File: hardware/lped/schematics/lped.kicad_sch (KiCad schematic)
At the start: 29 parts, among them J1 3V3, J10 SWDIO, J2 DOCK_BUTTON, J3 DOCK_CONN, J4 DOCK_LED, J5 GND, J6 ~{RESET}, J9 SWDCLK, U1 nRF52810-QCxx, Y1 32MHz

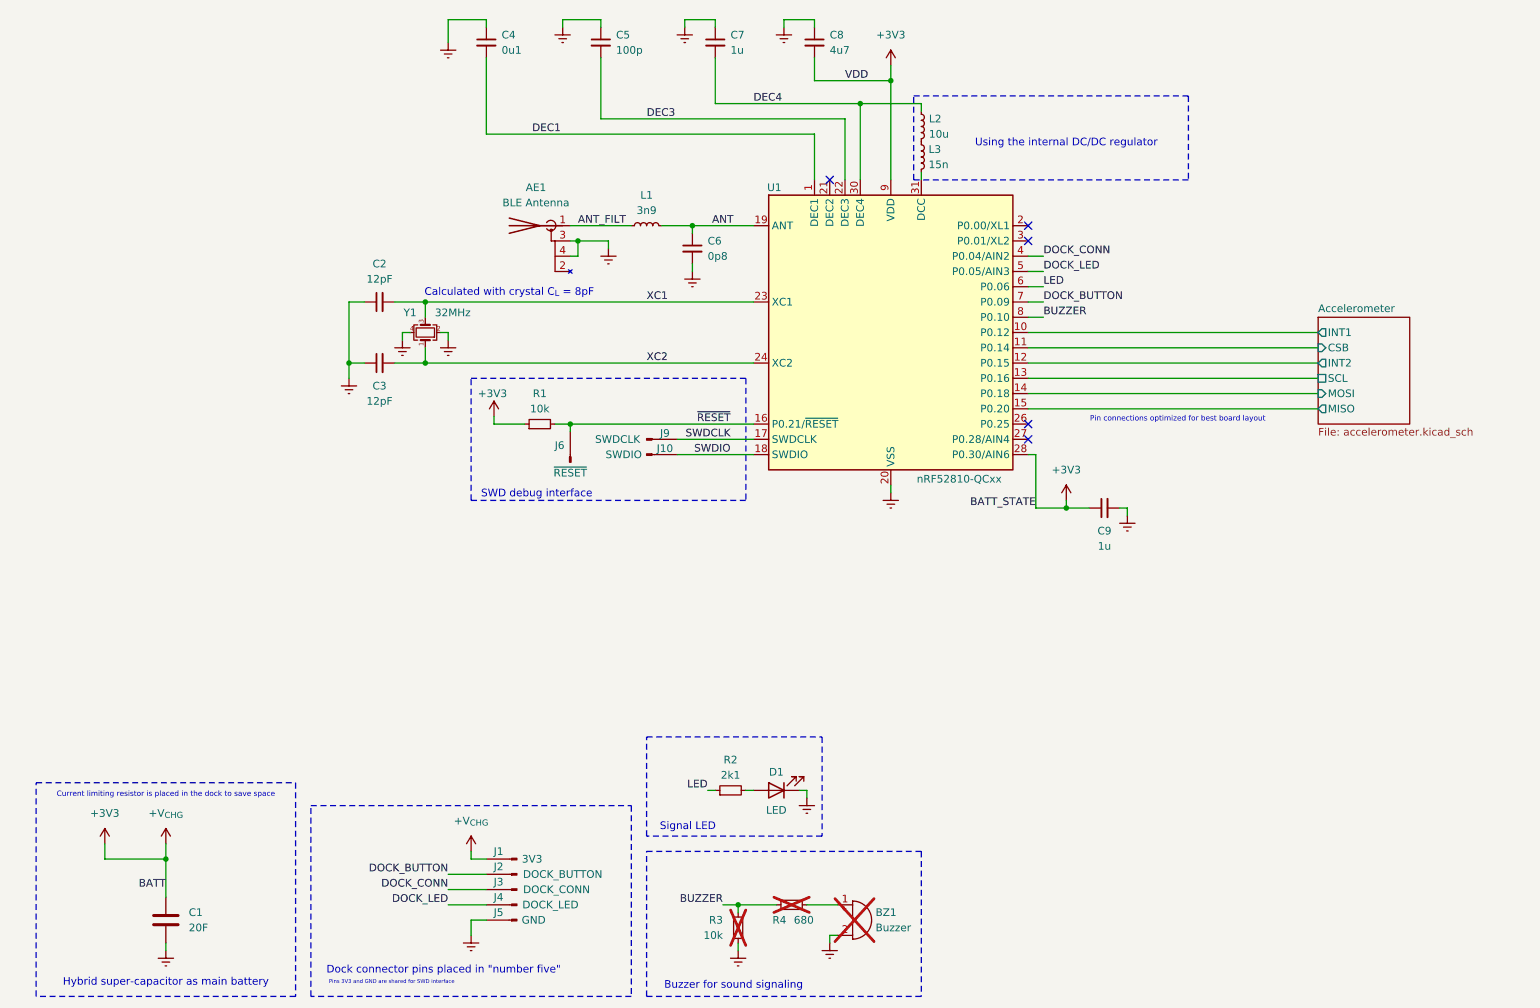
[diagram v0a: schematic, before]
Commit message: feat(hardware)!: v2 of LPED PCB
* Changed MCU to nRF52833 (from nRF52810)
* Added second LED
* Used specialized filter instead of discrete components for ANT
* Removed unnecessary pull-down resistor from miso
* Removed DOCK_BTN
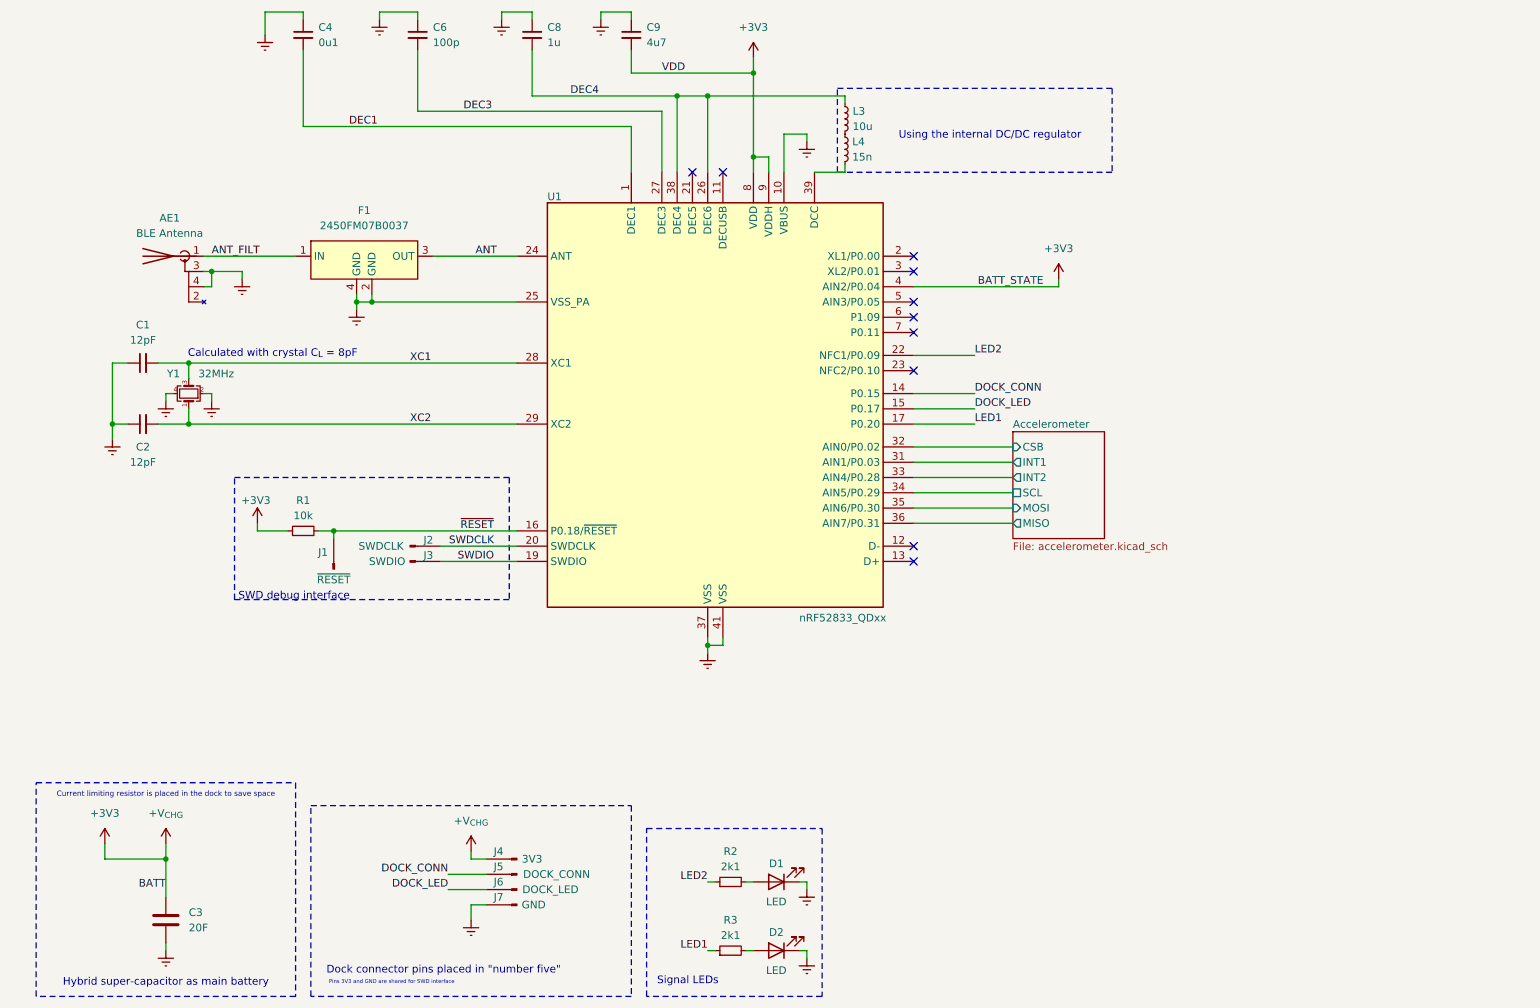
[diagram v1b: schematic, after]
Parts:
- removed BZ1: Buzzer, symbol Device:Buzzer
- removed C6: 0p8, Capacitor_SMD:C_0402_1005Metric, symbol Device:C_Small
- removed C9: 1u, Capacitor_SMD:C_0603_1608Metric, symbol Device:C_Small
- removed J2: DOCK_BUTTON, TestPoint:TestPoint_Pad_D2.0mm, symbol Connector:Conn_01x01_Pin
- removed L1: 3n9, Inductor_SMD:L_0402_1005Metric, symbol Device:L_Small
- removed R4: 680, Resistor_SMD:R_0402_1005Metric, symbol Device:R_Small
- removed U1: nRF52810-QCxx, Package_DFN_QFN:QFN-32-1EP_5x5mm_P0.5mm_EP3.6x3.6mm, symbol MCU_Nordic:nRF52810-QCxx
- added D2: LED, Diode_SMD:D_0805_2012Metric, symbol Device:LED
- added F1: 2450FM07B0037, RF_Filter:FIL_2450FM07D0034T, symbol Filter_Networks_Custom:2450FM07B0037
- added U1: nRF52833_QDxx, Package_DFN_QFN:QFN-40-1EP_5x5mm_P0.4mm_EP3.6x3.6mm, symbol MCU_Nordic:nRF52833_QDxx
- R3: value 10k -> 2k1; now fitted; now in the parts list
- renumbered C2 to C1, C3 to C2, C1 to C3, C5 to C6, C7 to C8, C8 to C9, J6 to J1, J9 to J2, J10 to J3, J1 to J4, J3 to J5, J4 to J6, J5 to J7, L2 to L3, L3 to L4
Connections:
- net +3V3: now also U1.18 (VDD), U1.30 (VDD), U1.4 (AIN2/P0.04), U1.40 (VDD), U1.8 (VDD), U1.9 (VDDH)
- net ANT: now also F1.3 (OUT), U1.24 (ANT)
- net ANT_FILT: now also F1.1 (IN)
- net Accelerometer/CSB: now also U1.32 (AIN0/P0.02)
- net Accelerometer/INT1: now also U1.31 (AIN1/P0.03)
- net Accelerometer/INT2: now also U1.33 (AIN4/P0.28)
- net Accelerometer/MISO: now also U1.36 (AIN7/P0.31)
- net Accelerometer/MOSI: now also U1.35 (AIN6/P0.30)
- net Accelerometer/SCL: now also U1.34 (AIN5/P0.29)
- net DEC1: now also U1.1 (DEC1)
- net DEC3: now also U1.27 (DEC3)
- net DEC4: now also U1.26 (DEC6), U1.38 (DEC4)
- net DOCK_CONN: now also U1.14 (P0.15)
- net DOCK_LED: now also U1.15 (P0.17)
- net Earth: now also D2.1 (K), F1.2 (GND), F1.4 (GND), U1.10 (VBUS), U1.25 (VSS_PA), U1.37 (VSS), U1.41 (VSS); no longer R3.1
- net SWDCLK: now also U1.20 (SWDCLK)
- net SWDIO: now also U1.19 (SWDIO)
- net XC1: now also U1.28 (XC1)
- net XC2: now also U1.29 (XC2)
- net ~{RESET}: now also U1.16 (P0.18/~{RESET})
- net at L4.2: now also U1.39 (DCC)
- net BUZZER: no longer names the net of R3.2
- net BUZZER: now also D2.2 (A)
- net LED renamed LED2
- net LED2: now also U1.22 (NFC1/P0.09)
- new net LED1: R3.1, U1.17 (P0.20)
- no-connect marks 5 -> 10
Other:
- note added: "Signal LEDs"
- note removed: "Buzzer for sound signaling"
- note removed: "Pin connections optimized for best board layout"
- note removed: "Signal LED"
- moved on the sheet: AE1, C1, C2, C4, C6, C8, C9, D1, J1, J2, J3, J5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

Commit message: feat(hardware): replaced LEDs on dice
* Replaced two red LEDs with single RGB LED (LTRB37G-4R4S)
* Added more ground vias
* Removed DOCK_LED
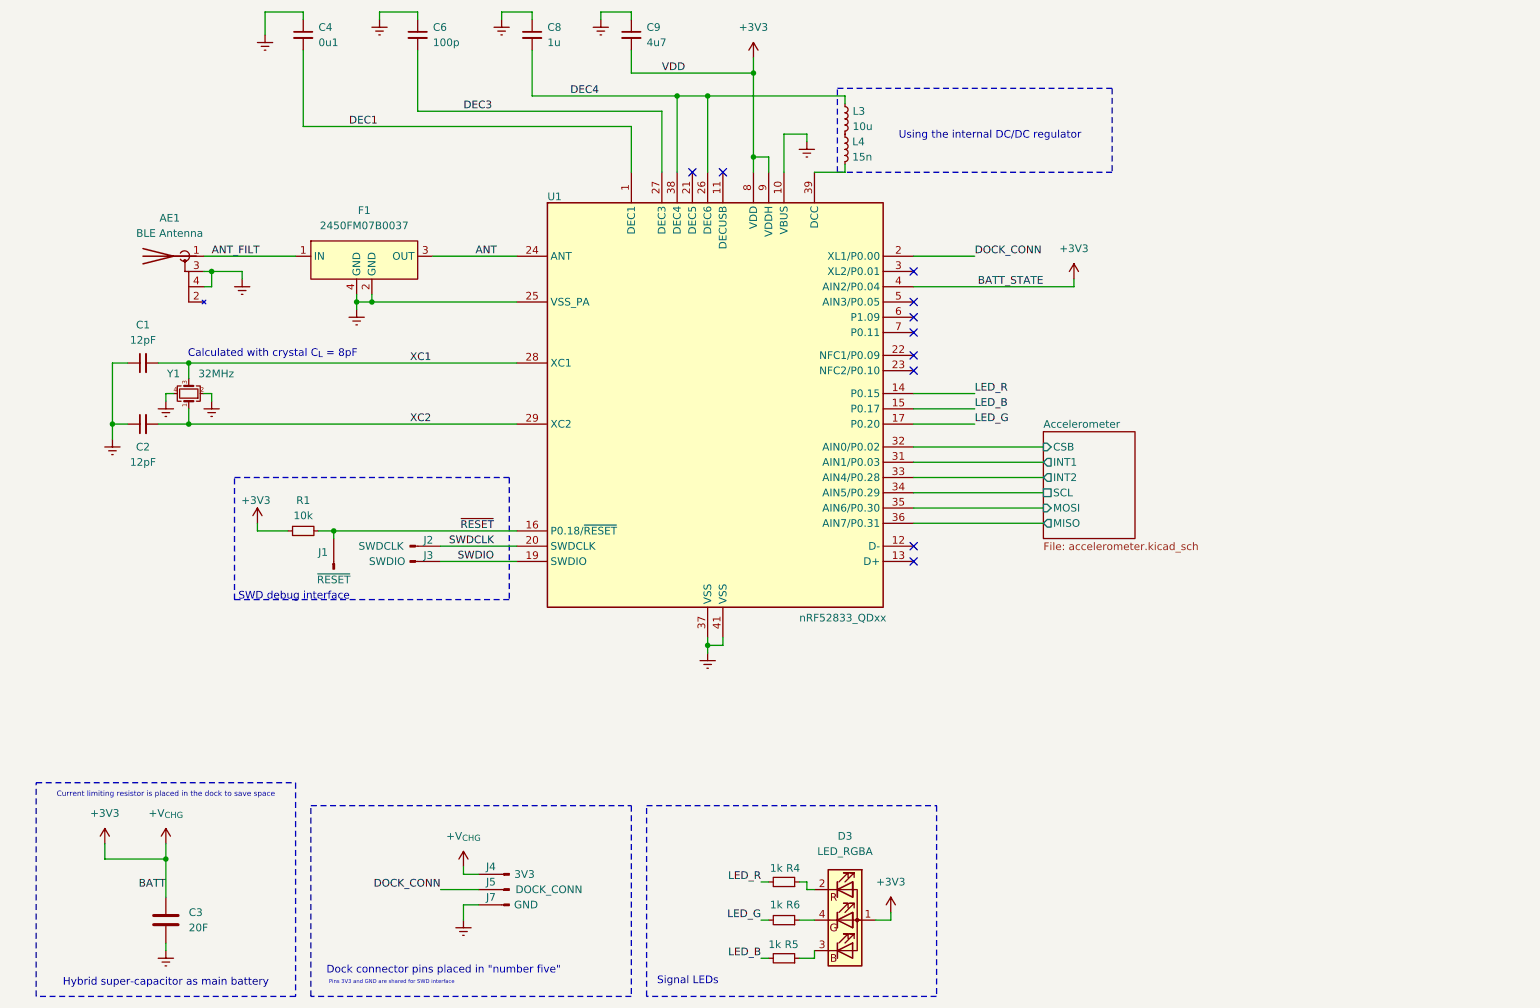
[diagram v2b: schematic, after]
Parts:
- removed D1, D2: LED, Diode_SMD:D_0805_2012Metric, symbol Device:LED
- removed J6: DOCK_LED, TestPoint:TestPoint_Pad_D2.0mm, symbol Connector:Conn_01x01_Pin
- removed R2, R3: 2k1, Resistor_SMD:R_0402_1005Metric, symbol Device:R_Small
- added D3: LED_RGBA, LED_SMD:LED_Wurth_150044M155260, symbol Device:LED_RGBA
- added R4, R5, R6: 1k, Resistor_SMD:R_0402_1005Metric, symbol Device:R_Small
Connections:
- net +3V3: now also D3.1 (A)
- net DOCK_CONN: now also U1.2 (XL1/P0.00); no longer U1.14 (P0.15)
- net DOCK_LED renamed LED_B
- net LED_B: now also R5.2
- net LED1 renamed LED_G
- net LED_G: now also R6.2
- net LED2: no longer names the net of U1.22 (NFC1/P0.09)
- new net: D3.2 (RK), R4.1
- new net: D3.3 (BK), R5.1
- new net: D3.4 (GK), R6.1
- new net LED_R: R4.2, U1.14 (P0.15)
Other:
- moved on the sheet: J4, J5, J7
